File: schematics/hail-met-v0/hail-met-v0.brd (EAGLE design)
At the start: 77.1 x 61 mm, 102 parts, among them IC1 MCP73871, J1 AVR_SPI_PRG_6PTH, U1 ATMEGA328P, Y1 16MHZ

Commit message: worked on routing
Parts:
- moved C8 57.4 mm to (65.2, 38.9), turned to 0 degrees
- moved C1 16.6 mm to (38.5, 29.7), turned to 0 degrees
- moved R1 6.09 mm to (10.9, 53.2), turned to 180 degrees
- moved AT_PINS 2.12 mm to (12.2, 36.4)
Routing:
- net SPKR_L+: track 0.00 -> 32.5 mm, vias 0 -> 2
- net N$8: track 0.00 -> 29.5 mm
- net SPKR_R+: track 0.00 -> 28.7 mm, vias 0 -> 2
- net MIC_R-: track 0.00 -> 28.0 mm
- net MIC_R+: track 0.00 -> 26.7 mm, vias 0 -> 2
- net N$12: track 0.00 -> 24.2 mm, vias 0 -> 2
- net N$14: track 0.00 -> 23.5 mm
- net N$5: track 0.00 -> 23.2 mm
- net N$7: track 0.00 -> 21.7 mm
- net MIC_L-: track 0.00 -> 20.0 mm, vias 0 -> 2
- net N$26: track 0.00 -> 19.8 mm
- net MIC_L+: track 0.00 -> 18.6 mm, vias 0 -> 2
- net LED_SDI: track 0.00 -> 17.4 mm, vias 0 -> 1
- net N$11: track 0.00 -> 16.9 mm, vias 0 -> 2
- net N$6: track 0.00 -> 14.6 mm
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
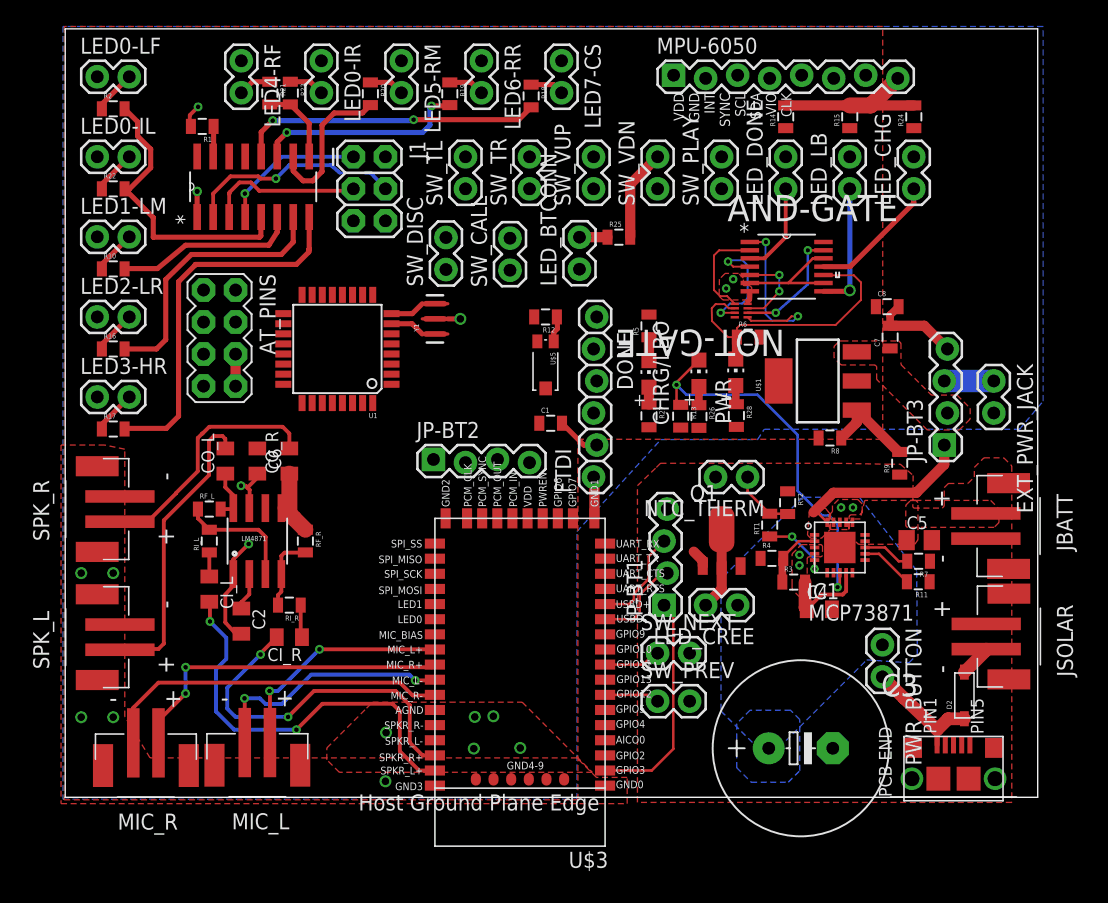
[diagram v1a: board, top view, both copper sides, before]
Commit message: finished initial PCB routing/layout
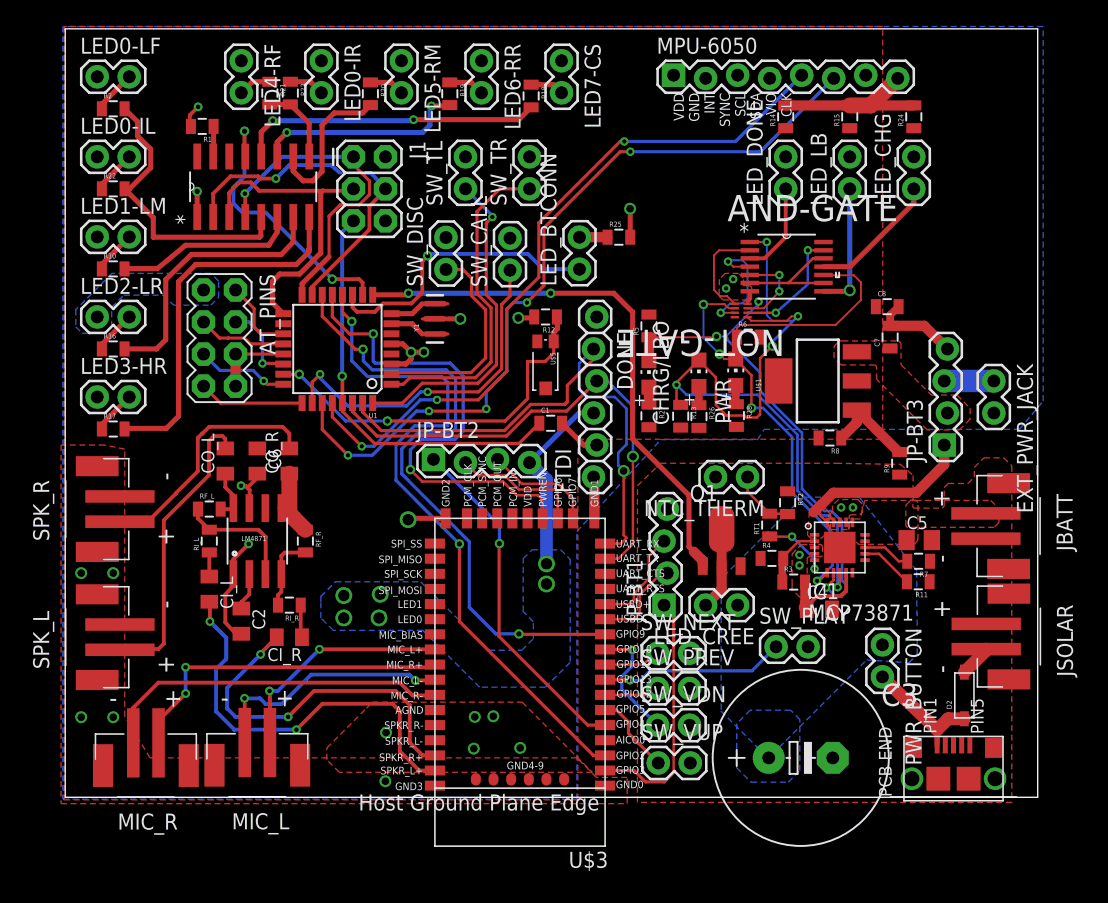
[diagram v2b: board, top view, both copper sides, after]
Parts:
- moved SW_VUP 45.8 mm to (47.0, 2.72), turned to 0 degrees
- moved SW_VDN 42.5 mm to (47.0, 5.71), turned to 0 degrees
- moved SW_PLAY 36.6 mm to (56.4, 11.9), turned to 0 degrees
- moved SW_PREV 1.02 mm to (47.0, 8.64)
- moved C3 0.76 mm to (58.3, 3.12)
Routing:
- net MPU_SDA: track 0.00 -> 62.3 mm, vias 0 -> 5
- net MPU_SCL: track 0.00 -> 57.0 mm, vias 0 -> 3
- net BT_EVENT: track 0.00 -> 54.1 mm, vias 0 -> 2
- net BT_CMD: track 0.00 -> 50.2 mm, vias 0 -> 2
- net TXD: track 0.00 -> 44.3 mm, vias 0 -> 1
- net LED_CREE: track 1.44 -> 43.7 mm, vias 0 -> 2
- net RXD: track 0.00 -> 40.0 mm, vias 0 -> 1
- net DEV_EN: track 0.00 -> 39.0 mm, vias 0 -> 2
- net CHG_STAT2: track 8.60 -> 46.9 mm, vias 2 -> 5
- net RESET: track 0.00 -> 32.8 mm, vias 0 -> 1
- net AMB_IN: track 2.08 -> 30.0 mm, vias 0 -> 2
- net BT_GPIO4: track 0.00 -> 27.5 mm, vias 0 -> 1
- net SW_CALL: track 0.00 -> 27.5 mm, vias 0 -> 2
- net SW_TL: track 0.00 -> 26.5 mm, vias 0 -> 1
- net SW_TR: track 0.00 -> 25.9 mm
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- added copper zone on layer 16, net 3.3V

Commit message: added headlight code (NEED TEST) and updated pcb
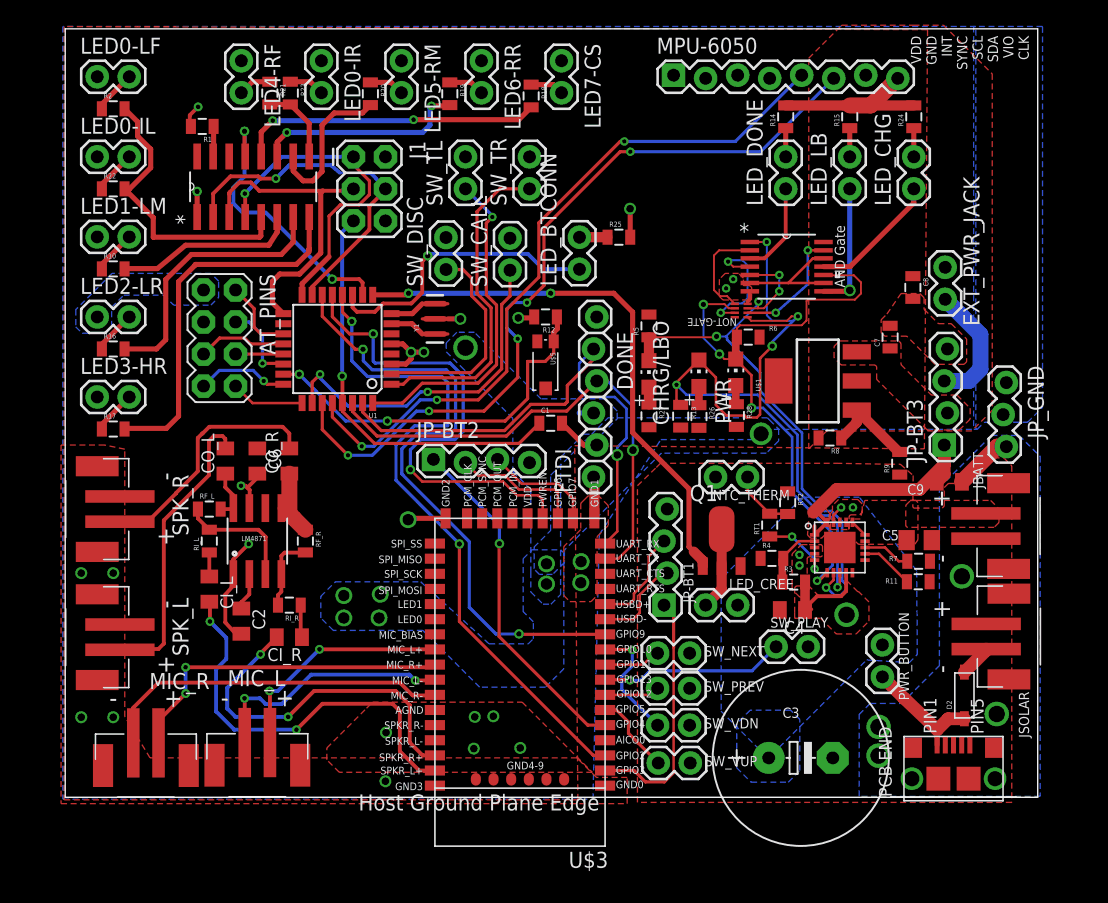
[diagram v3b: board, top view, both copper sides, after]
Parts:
- added C9: 10uF, adafruit:C0805K
- added JP_GND: (no value), SparkFun-Connectors:1X03_LOCK
- moved EXT_PWR_JACK 7.54 mm to (69.8, 39.5), turned to 90 degrees
- moved C8 2.54 mm to (67.2, 40.4), turned to 270 degrees
- moved C4 2.13 mm to (57.7, 14.9), turned to 180 degrees
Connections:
- net AREF: now also AT_PINS.5; no longer AT_PINS.3
- net CHG_VOUT: now also C9.1
- net GND: now also AT_PINS.3, C9.2, JP_GND.1, JP_GND.2, JP_GND.3; no longer AT_PINS.8
- net PC1: now also AT_PINS.7; no longer AT_PINS.5
- net PC2: now also AT_PINS.8; no longer AT_PINS.7
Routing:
- net 3.3V: track 15.3 -> 1.14 mm, vias 6 -> 8
- net EXT_5V: track 3.94 -> 9.95 mm
- net CHG_VOUT: track 14.9 -> 20.2 mm
- net GND: track 62.2 -> 57.2 mm, vias 22 -> 28
- net PC2: track 8.37 -> 5.83 mm
- net N$30: track 0.00 -> 2.28 mm
- net N$24: track 0.00 -> 2.28 mm
- net N$22: track 0.00 -> 2.28 mm
- net VCHG: track 7.89 -> 9.53 mm, vias 4 -> 5
- net VBATT: track 0.00 -> 1.44 mm
- net TXD: track 44.3 -> 43.1 mm
- net MPU_SDA: track 62.3 -> 63.0 mm
- net CHG_PG: track 49.3 -> 49.9 mm
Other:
- board text added: "AND Gate"

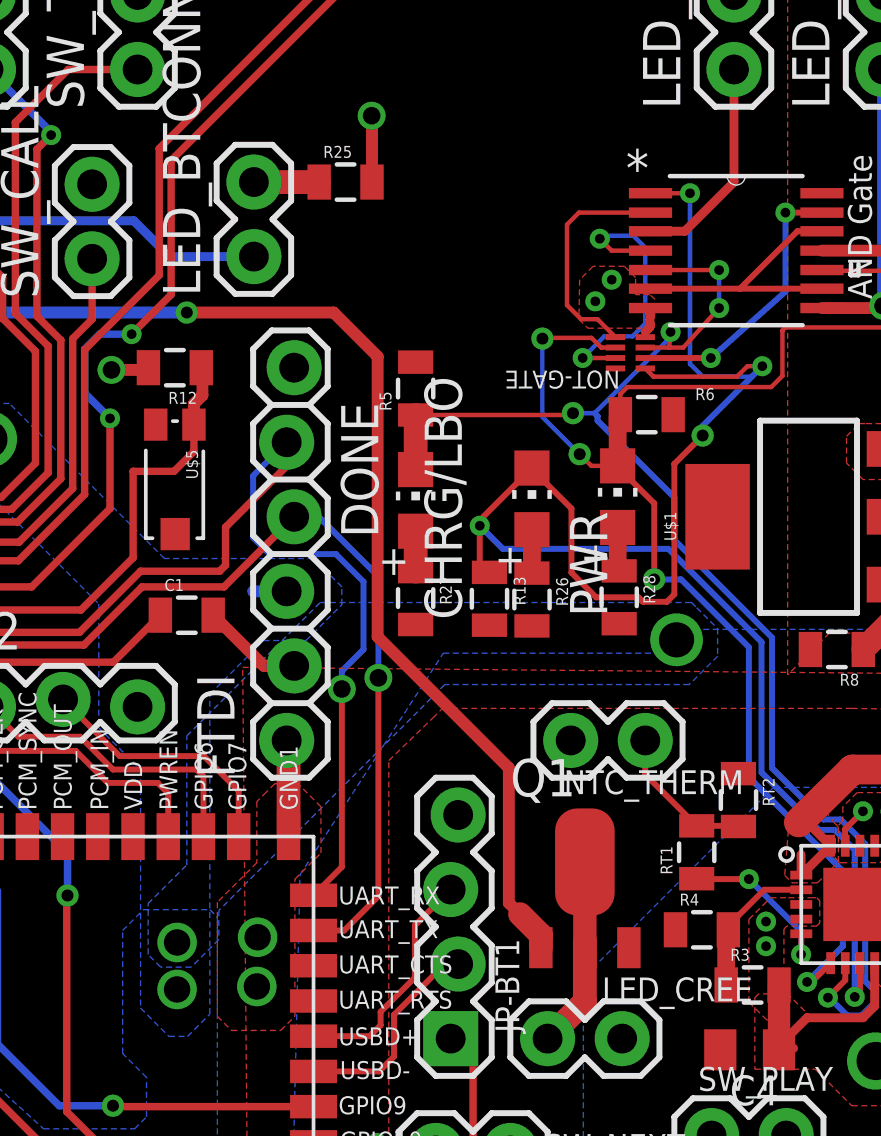
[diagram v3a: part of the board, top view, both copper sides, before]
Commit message: added pull-down for transistor
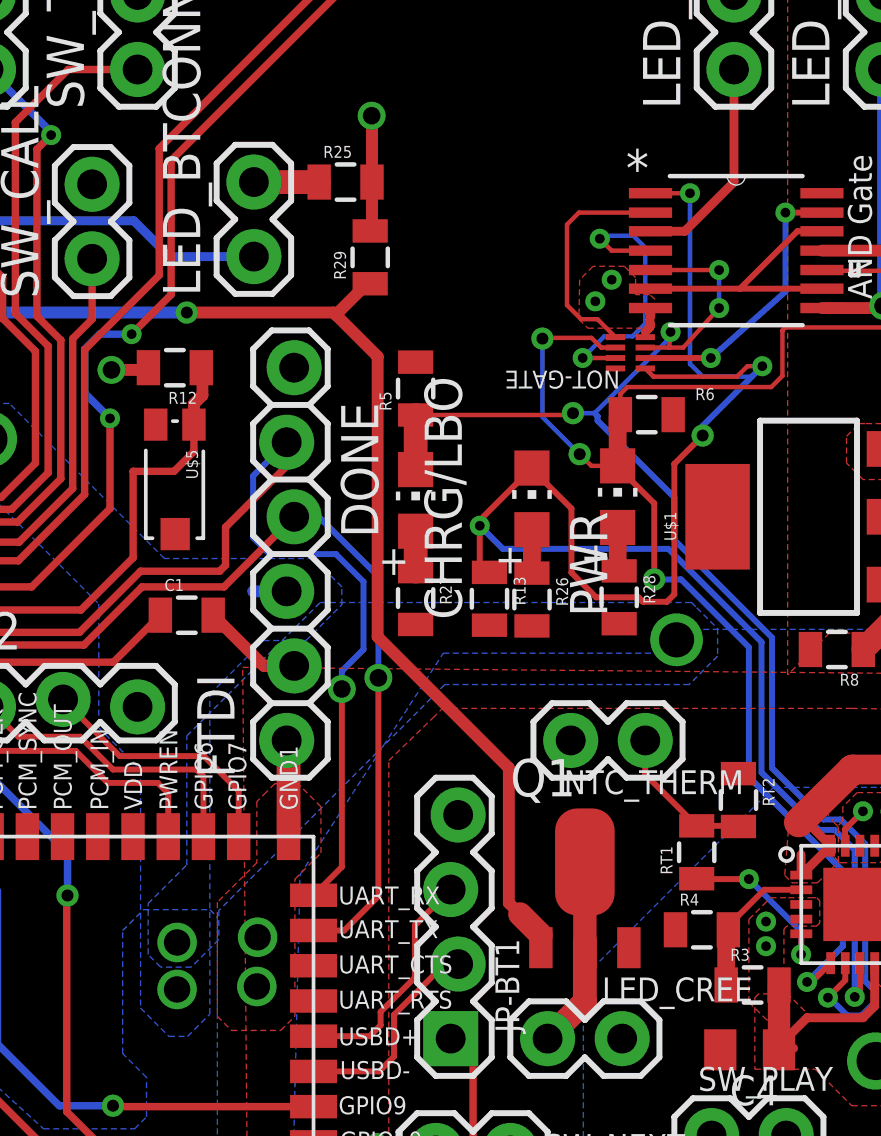
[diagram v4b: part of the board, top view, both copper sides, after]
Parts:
- added R29: 10K, SparkFun-Passives:0805
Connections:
- net GND: now also R29.2
- net LED_CREE: now also R29.1
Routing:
- net GND: track 57.2 -> 58.9 mm
- net LED_CREE: track 43.7 -> 44.9 mm
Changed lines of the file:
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@@
 <layer number="18" name="Vias" color="2" fill="1" visible="yes" active="yes"/>
 <layer number="19" name="Unrouted" color="6" fill="1" visible="yes" active="yes"/>
-<layer number="20" name="Dimension" color="15" fill="1" visible="yes" active="yes"/>
+<layer number="20" name="Dimension" color="15" fill="1" visible="no" active="yes"/>
 <layer number="21" name="tPlace" color="7" fill="1" visible="yes" active="yes"/>
 <layer number="22" name="bPlace" color="7" fill="1" visible="no" active="yes"/>
@@
 <attribute name="SUPPLIER" value="Texas Instruments" x="19.3548" y="50.8254" size="1.778" layer="27" rot="R90" display="off"/>
 <attribute name="OC_FARNELL" value="1755251" x="19.3548" y="50.8254" size="1.778" layer="27" rot="R90" display="off"/>
-<attribute name="VALUE" x="23.0124" y="42.9006" size="2.0828" layer="27" ratio="10" rot="SR90"/>
 </element>
 <element name="Y1" library="SparkFun-FreqCtrl" package="RESONATOR-SMD" value="16MHZ" x="29.337" y="37.9476" rot="R90">
@@
 <attribute name="VALUE" x="65.4464" y="23.0174" size="0.8128" layer="27"/>
 </element>
+<element name="R29" library="SparkFun-Passives" package="0805" value="10K" x="44.7548" y="41.8592" rot="R90"/>
 </elements>
 <signals>
@@
 <via x="40.9194" y="18.6944" extent="1-16" drill="0.9" shape="octagon"/>
 <via x="40.894" y="17.018" extent="1-16" drill="0.9" shape="octagon"/>
+<contactref element="R29" pad="2"/>
+<wire x1="44.8166" y1="44.4246" x2="44.8166" y2="42.821" width="0.4064" layer="1"/>
+<wire x1="44.8166" y1="42.821" x2="44.7548" y2="42.7592" width="0.4064" layer="1"/>
 <wire x1="74.6506" y1="27.813" x2="74.3966" y2="30.353" width="0" layer="19" extent="1-1"/>
 </signal>
@@
 </signal>
 <signal name="LED_CREE">
-<contactref element="Q1" pad="1"/>
 <contactref element="U1" pad="9"/>
-<wire x1="50.571" y1="18.339" x2="50.571" y2="18.771" width="0.8128" layer="1"/>
 <wire x1="50.571" y1="18.771" x2="49.8602" y2="19.4818" width="0.8128" layer="1"/>
 <wire x1="49.8602" y1="19.4818" x2="49.4792" y2="19.8628" width="0.4064" layer="1"/>
@@
 <wire x1="49.4792" y1="24.4602" x2="45.0088" y2="28.9306" width="0.4064" layer="1"/>
 <wire x1="45.0088" y1="28.9306" x2="45.0088" y2="38.481" width="0.4064" layer="1"/>
-<wire x1="45.0088" y1="38.481" x2="43.5102" y2="39.9796" width="0.4064" layer="1"/>
+<wire x1="45.0088" y1="38.481" x2="43.5864" y2="39.9034" width="0.4064" layer="1"/>
+<wire x1="43.5864" y1="39.9034" x2="43.5102" y2="39.9796" width="0.4064" layer="1"/>
 <wire x1="43.5102" y1="39.9796" x2="38.5064" y2="39.9796" width="0.4064" layer="1"/>
 <via x="38.5064" y="39.9796" extent="1-16" drill="0.4064"/>
@@
 <wire x1="27.2288" y1="39.9796" x2="27.1018" y2="39.8526" width="0.4064" layer="1"/>
 <wire x1="27.1018" y1="39.8526" x2="24.39" y2="39.8526" width="0.4064" layer="1"/>
+<contactref element="Q1" pad="1"/>
+<contactref element="R29" pad="1"/>
+<wire x1="44.7548" y1="40.9592" x2="44.6422" y2="40.9592" width="0.4064" layer="1"/>
+<wire x1="44.6422" y1="40.9592" x2="43.5864" y2="39.9034" width="0.4064" layer="1"/>
+<wire x1="50.571" y1="18.771" x2="50.571" y2="18.339" width="0" layer="19" extent="1-1"/>
 </signal>
 <signal name="PC1">

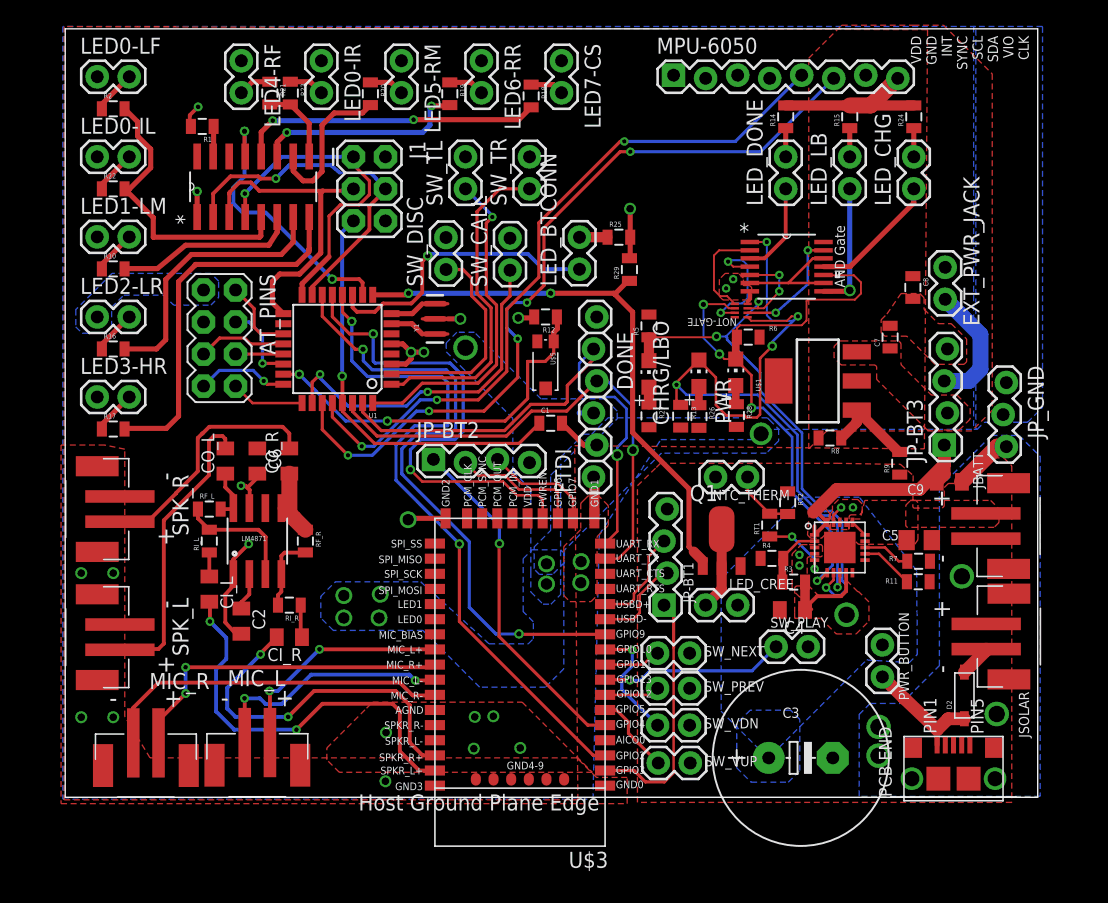
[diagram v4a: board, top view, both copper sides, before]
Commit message: added some decoupling caps to the board, prep for ben
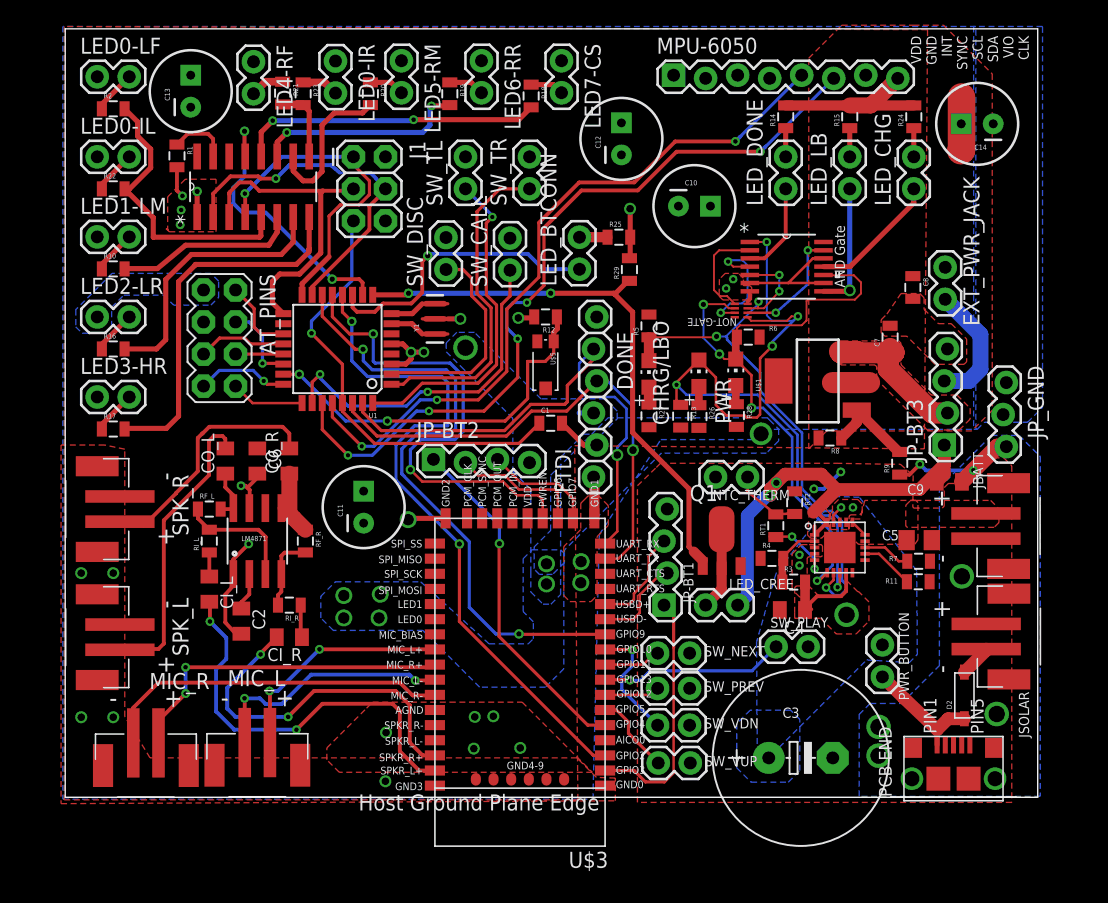
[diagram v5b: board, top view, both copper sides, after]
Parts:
- added C10, C11, C12, C13, C14: (no value), SparkFun-Capacitors:CPOL-RADIAL-100UF-25V
- moved R1 3.08 mm to (8.86, 50.9), turned to 270 degrees
- moved LED0-IR 1.12 mm to (21.4, 58.4)
- moved R23 1.02 mm to (18.9, 55.8)
- moved R21 1.02 mm to (17.2, 55.9)
- moved LED4-RF 0.97 mm to (14.9, 58.3)
- moved RT2 0.56 mm to (57.9, 23.4)
- moved RT1 0.49 mm to (56.4, 21.5)
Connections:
- net 3.3V: now also C10.1, C11.1, C12.1, C13.1, C14.1
- net CHG_VOUT: now also LED_CREE.1
- net GND: now also C10.2, C11.2, C12.2, C13.2, C14.2
- net VCHG: no longer LED_CREE.1
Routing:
- net CHG_VOUT: track 20.2 -> 38.1 mm, vias 0 -> 2
- net VIN: track 0.00 -> 14.0 mm
- net GND: track 58.9 -> 68.5 mm, vias 28 -> 34
- net 3.3V: track 1.14 -> 8.38 mm
- net N$56: track 2.40 -> 4.84 mm
- net RESET: track 32.8 -> 34.8 mm
